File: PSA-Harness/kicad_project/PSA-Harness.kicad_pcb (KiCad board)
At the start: 4 copper layers, 57.4 x 53.6 mm, 15 parts, among them J1 to_EPS_1, J10 B2B_1, J11 B2B_2, J2 to_EPS_2, J3 to_ESP_3, J4 to_car_1, J5 to_car_2, J6 to_car_3, J7 USB_C_Receptacle, J8 B2B_1, J9 B2B_2, K1 G6K-2G-Y DC5

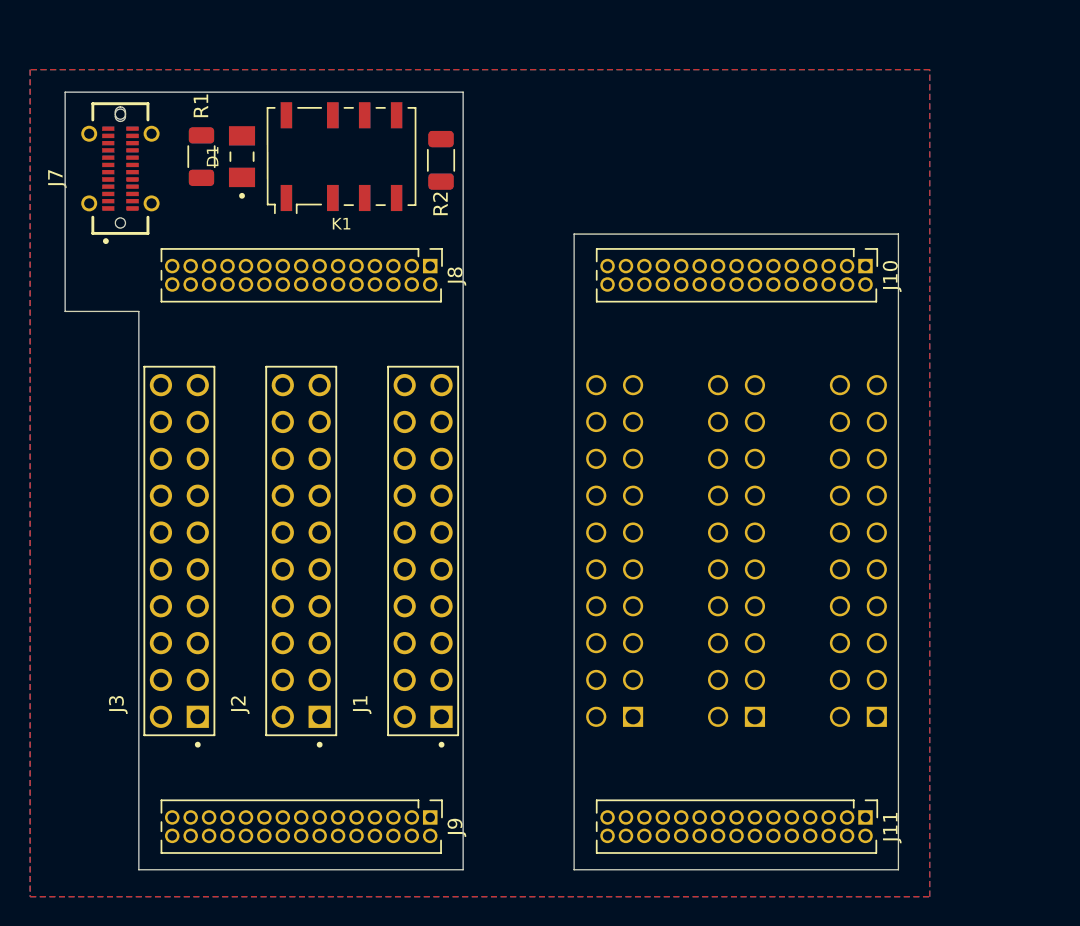
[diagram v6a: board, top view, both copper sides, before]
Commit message: chg: final PCB shape
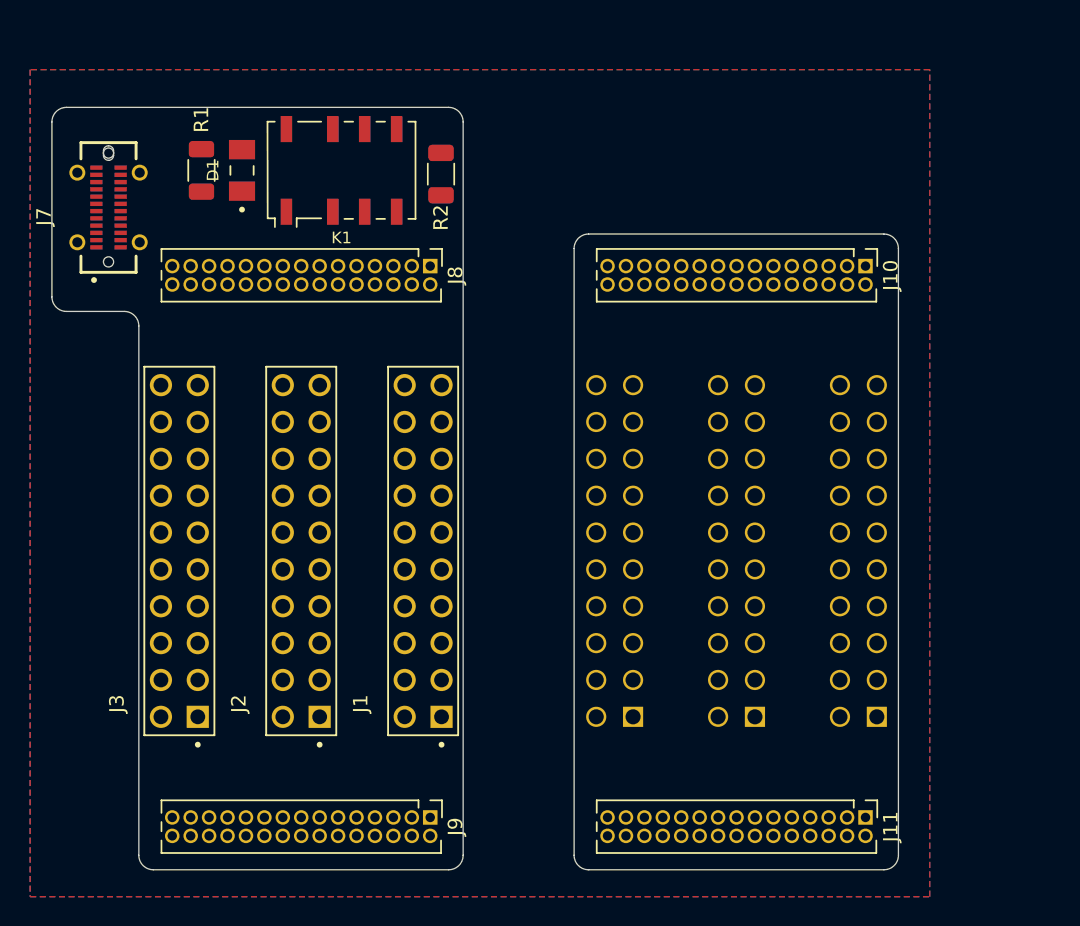
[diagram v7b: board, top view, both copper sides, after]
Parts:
- moved J7 2.80 mm to (92.4, 98.5)
- moved D1 0.95 mm to (101.6, 95.9)
- moved K1 0.95 mm to (108.5, 95.9)
- moved R1 0.95 mm to (98.8, 95.9)
- moved R2 0.95 mm to (115.3, 96.2)
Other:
- board size 57.4 x 53.6 mm -> 58.3 x 52.5 mm
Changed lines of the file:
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@@
 	(footprint "Resistor_SMD:R_1206_3216Metric"
 		(layer "F.Cu")
-		(at 98.806 94.996 -90)
+		(at 98.806 95.946 -90)
 		(descr "Resistor SMD 1206 (3216 Metric), square (rectangular) end terminal, IPC_7351 nominal, (Body size source: IPC-SM-782 page 72, https://www.pcb-3d.com/wordpress/wp-content/uploads/ipc-sm-782a_amendment_1_and_2.pdf), generated with kicad-footprint-generator")
 		(tags "resistor")
@@
 	(footprint "Resistor_SMD:R_1206_3216Metric"
 		(layer "F.Cu")
-		(at 115.316 95.25 -90)
+		(at 115.316 96.2 -90)
 		(descr "Resistor SMD 1206 (3216 Metric), square (rectangular) end terminal, IPC_7351 nominal, (Body size source: IPC-SM-782 page 72, https://www.pcb-3d.com/wordpress/wp-content/uploads/ipc-sm-782a_amendment_1_and_2.pdf), generated with kicad-footprint-generator")
 		(tags "resistor")
@@
 	(footprint "PSA:GCT_USB4115-03-C_REVB4"
 		(layer "F.Cu")
-		(at 93.218 95.818 90)
+		(at 92.4 98.5 90)
 		(property "Reference" "J7"
 			(at -0.635 -4.445 90)
@@
 			(polygon
 				(pts
-					(xy 91.418 96.618) (xy 91.418 95.018) (xy 90.718 95.018) (xy 90.718 96.618)
+					(xy 90.6 99.3) (xy 90.6 97.7) (xy 89.9 97.7) (xy 89.9 99.3)
 				)
 			)
@@
 			(polygon
 				(pts
-					(xy 95.018 96.618) (xy 95.018 95.018) (xy 95.718 95.018) (xy 95.718 96.618)
+					(xy 94.2 99.3) (xy 94.2 97.7) (xy 94.9 97.7) (xy 94.9 99.3)
 				)
 			)
@@
 			(polygon
 				(pts
-					(xy 91.418 96.618) (xy 91.418 95.018) (xy 90.718 95.018) (xy 90.718 96.618)
+					(xy 90.6 99.3) (xy 90.6 97.7) (xy 89.9 97.7) (xy 89.9 99.3)
 				)
 			)
@@
 			(polygon
 				(pts
-					(xy 95.018 96.618) (xy 95.018 95.018) (xy 95.718 95.018) (xy 95.718 96.618)
+					(xy 94.2 99.3) (xy 94.2 97.7) (xy 94.9 97.7) (xy 94.9 99.3)
 				)
 			)
@@
 	(footprint "Relay_SMD:Relay_DPDT_Omron_G6K-2G-Y"
 		(layer "F.Cu")
-		(at 108.458 94.996 90)
+		(at 108.458 95.946 90)
 		(descr "Omron G6K-2G-Y relay package http://omronfs.omron.com/en_US/ecb/products/pdf/en-g6k.pdf")
 		(tags "Omron G6K-2G-Y relay")
@@
 	(footprint "PSA:DIO_BAV21W_RHG"
 		(layer "F.Cu")
-		(at 101.6 94.996 90)
+		(at 101.6 95.946 90)
 		(property "Reference" "D1"
 			(at 0 -2 90)
@@
 	)
 	(gr_line
-		(start 116.84 90.551)
-		(end 116.84 144.145)
+		(start 116.84 92.6)
+		(end 116.84 143.145)
+		(stroke
+			(width 0.05)
+			(type default)
+		)
+		(layer "Edge.Cuts")
+	)
+	(gr_arc
+		(start 145.84 100.33)
+		(mid 146.547107 100.622893)
+		(end 146.84 101.33)
+		(stroke
+			(width 0.05)
+			(type default)
+		)
+		(layer "Edge.Cuts")
+	)
+	(gr_arc
+		(start 116.84 143.145)
+		(mid 116.547107 143.852107)
+		(end 115.84 144.145)
 		(stroke
 			(width 0.05)
@@
 	)
 	(gr_line
-		(start 124.488 144.145)
-		(end 124.488 100.33)
+		(start 124.488 143.145)
+		(end 124.488 101.33)
+		(stroke
+			(width 0.05)
+			(type default)
+		)
+		(layer "Edge.Cuts")
+	)
+	(gr_arc
+		(start 115.84 91.6)
+		(mid 116.547107 91.892893)
+		(end 116.84 92.6)
 		(stroke
 			(width 0.05)
@@
 	)
 	(gr_line
-		(start 146.84 100.33)
-		(end 146.84 144.145)
+		(start 146.84 101.33)
+		(end 146.84 143.145)
 		(stroke
 			(width 0.05)
@@
 	)
 	(gr_line
-		(start 116.84 144.145)
-		(end 94.488 144.145)
+		(start 115.84 144.145)
+		(end 95.488 144.145)
 		(stroke
 			(width 0.05)
@@
 	)
 	(gr_line
-		(start 89.408 90.551)
-		(end 116.84 90.551)
+		(start 89.5 91.6)
+		(end 115.84 91.6)
+		(stroke
+			(width 0.05)
+			(type default)
+		)
+		(layer "Edge.Cuts")
+	)
+	(gr_arc
+		(start 88.5 92.6)
+		(mid 88.792893 91.892893)
+		(end 89.5 91.6)
+		(stroke
+			(width 0.05)
+			(type default)
+		)
+		(layer "Edge.Cuts")
+	)
+	(gr_arc
+		(start 124.488 101.33)
+		(mid 124.780893 100.622893)
+		(end 125.488 100.33)
 		(stroke
 			(width 0.05)
@@
 	)
 	(gr_line
-		(start 94.488 105.664)
-		(end 89.408 105.664)
+		(start 93.488 105.664)
+		(end 89.5 105.664)
+		(stroke
+			(width 0.05)
+			(type default)
+		)
+		(layer "Edge.Cuts")
+	)
+	(gr_arc
+		(start 125.488 144.145)
+		(mid 124.780893 143.852107)
+		(end 124.488 143.145)
 		(stroke
 			(width 0.05)
@@
 	)
 	(gr_line
-		(start 124.488 100.33)
-		(end 146.84 100.33)
+		(start 125.488 100.33)
+		(end 145.84 100.33)
 		(stroke
 			(width 0.05)
@@
 	)
 	(gr_line
-		(start 146.84 144.145)
-		(end 124.488 144.145)
+		(start 145.84 144.145)
+		(end 125.488 144.145)
+		(stroke
+			(width 0.05)
+			(type default)
+		)
+		(layer "Edge.Cuts")
+	)
+	(gr_arc
+		(start 146.84 143.145)
+		(mid 146.547107 143.852107)
+		(end 145.84 144.145)
+		(stroke
+			(width 0.05)
+			(type default)
+		)
+		(layer "Edge.Cuts")
+	)
+	(gr_arc
+		(start 89.5 105.664)
+		(mid 88.792893 105.371107)
+		(end 88.5 104.664)
 		(stroke
 			(width 0.05)
@@
 	)
 	(gr_line
-		(start 94.488 144.145)
-		(end 94.488 105.664)
+		(start 94.488 143.145)
+		(end 94.488 106.664)
 		(stroke
 			(width 0.05)
@@
 	)
 	(gr_line
-		(start 89.408 105.664)
-		(end 89.408 90.551)
+		(start 88.5 104.664)
+		(end 88.5 92.6)
+		(stroke
+			(width 0.05)
+			(type default)
+		)
+		(layer "Edge.Cuts")
+	)
+	(gr_arc
+		(start 93.488 105.664)
+		(mid 94.195107 105.956893)
+		(end 94.488 106.664)
+		(stroke
+			(width 0.05)
+			(type default)
+		)
+		(layer "Edge.Cuts")
+	)
+	(gr_arc
+		(start 95.488 144.145)
+		(mid 94.780893 143.852107)
+		(end 94.488 143.145)
 		(stroke
 			(width 0.05)

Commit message: cleared DRC errors
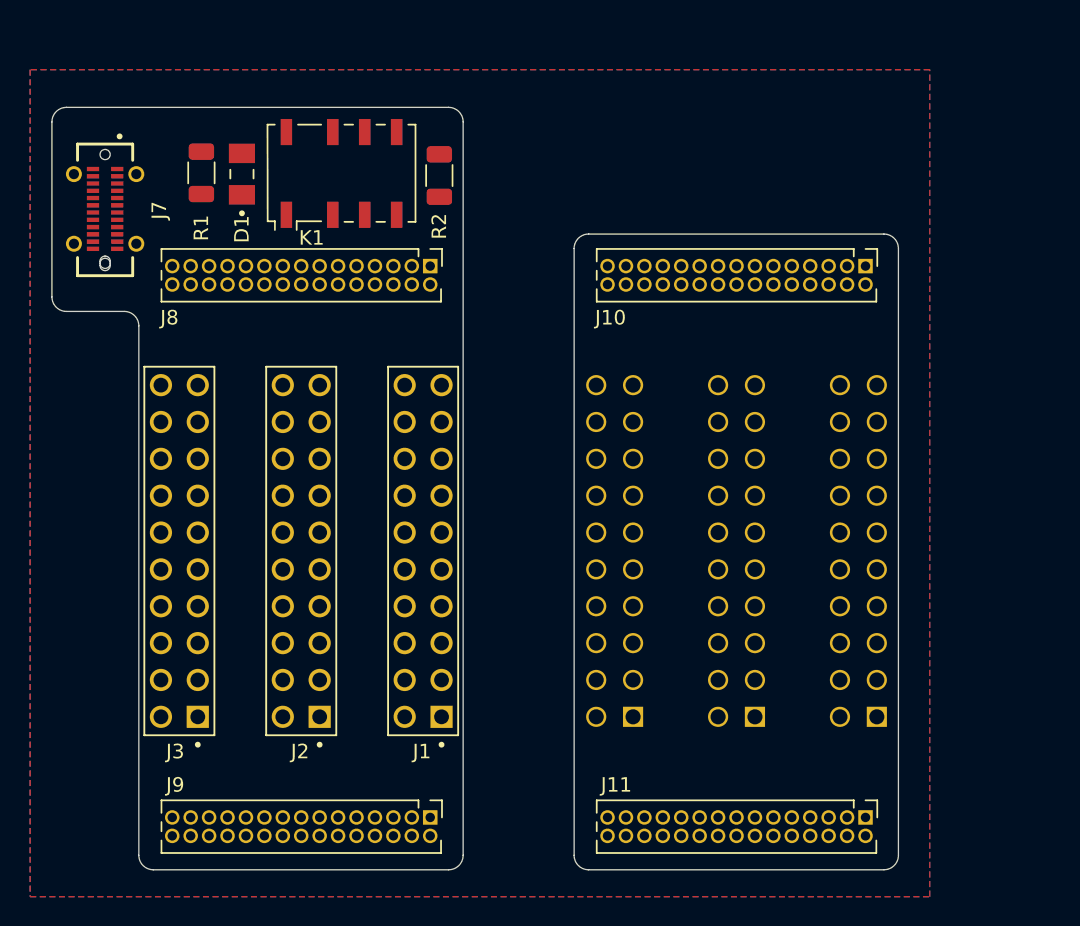
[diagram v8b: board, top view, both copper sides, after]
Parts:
- J7: value USB_C_Receptacle -> USB-C
- moved J7 0.26 mm to (92.2, 98.6), turned to -90 degrees
- moved D1 0.25 mm to (101.6, 96.2)
- moved K1 0.20 mm to (108.5, 96.2)
- moved R1 0.17 mm to (98.8, 96.1)
- moved R2 0.15 mm to (115.2, 96.3)
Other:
- rule pad_to_mask_clearance: 0 -> 0.038
